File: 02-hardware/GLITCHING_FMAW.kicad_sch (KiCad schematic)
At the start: 72 parts, among them J1 USB_C_Receptacle_USB2.0_16P, J2 AIN, J3 GLITCH, J4 ANA1, J5 ANA2, J6 ANA3, J7 GND, Q2 IRLB8721PBF, U1 TLV76133, U2 TLV76133, U3 LM358, U4 RP2040, U5 W25Q128JVS, U6 MS9280, Y1 12MHz

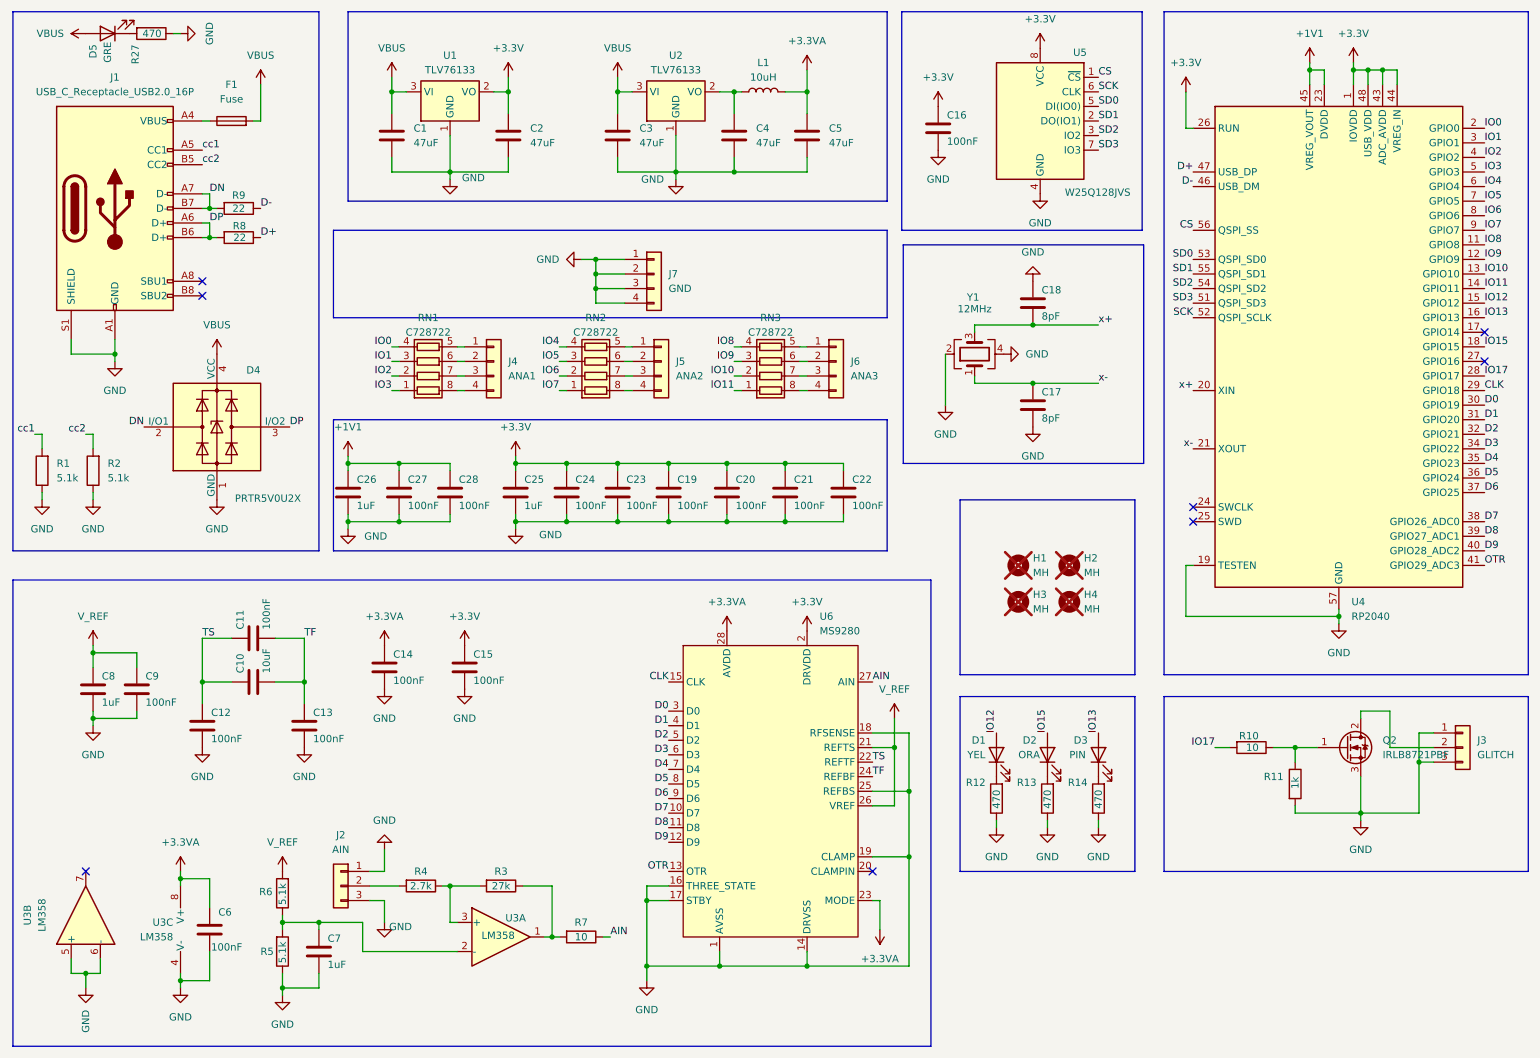
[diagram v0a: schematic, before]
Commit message: update hw to mosfet | update expamples
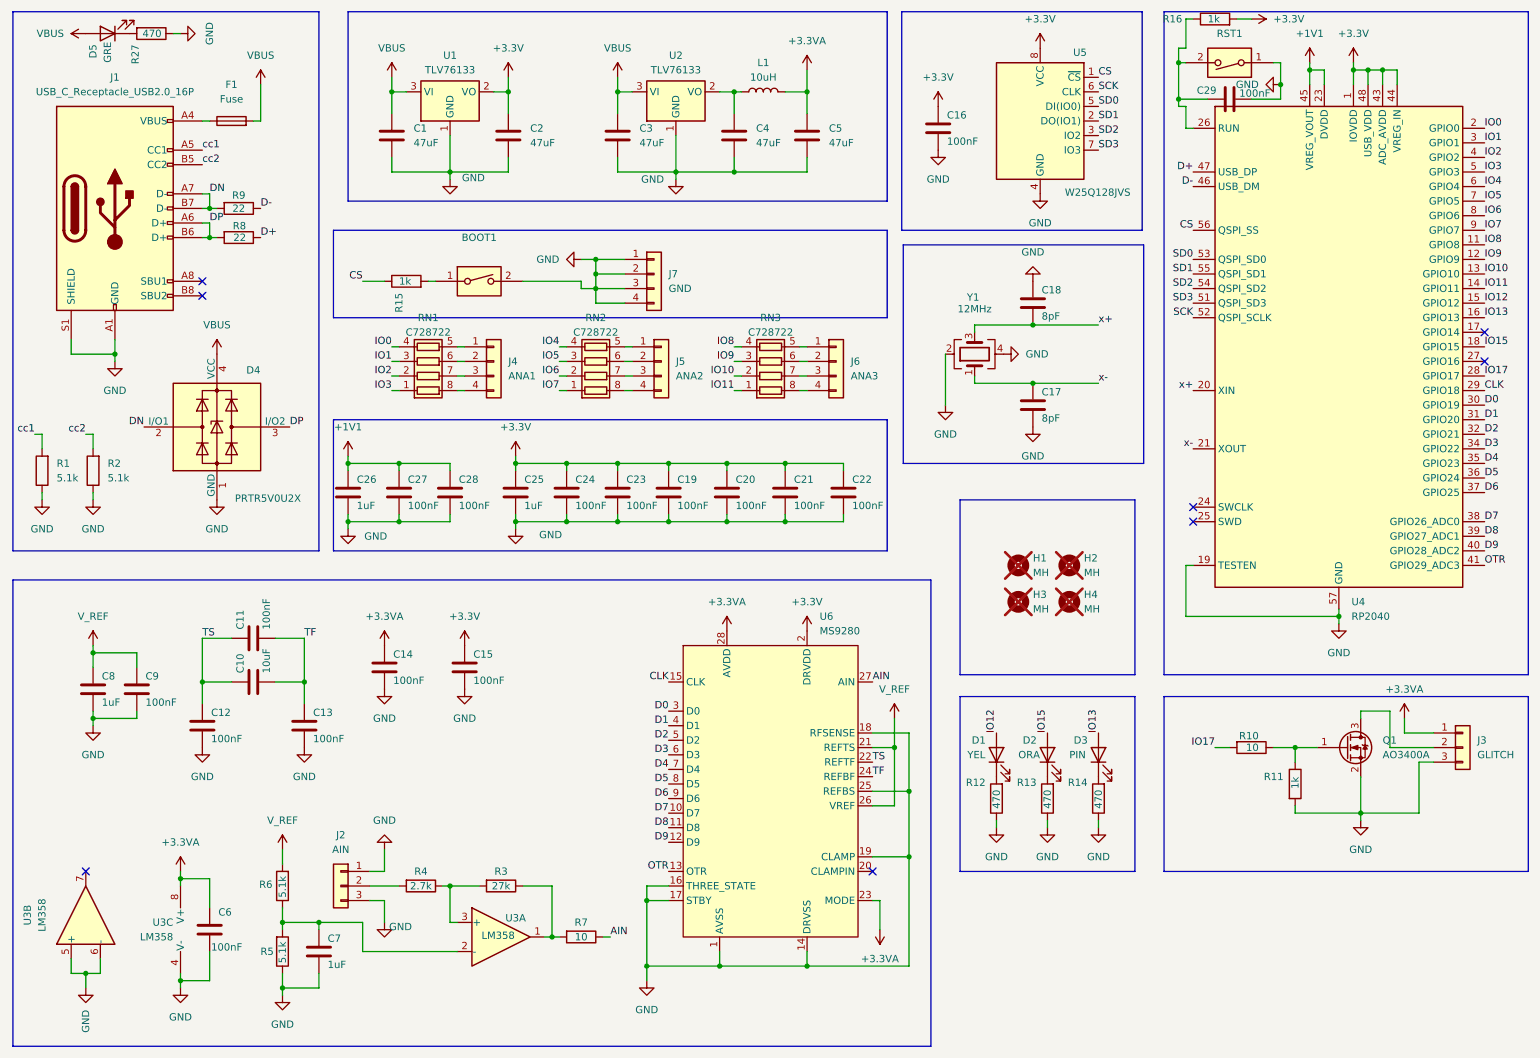
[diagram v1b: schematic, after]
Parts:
- removed Q2: IRLB8721PBF, Package_TO_SOT_SMD:SOT-223-3_TabPin2, symbol Transistor_FET:IRLB8721PBF
- added BOOT1, RST1: SW_DIP_x01, Button_Switch_SMD:SW_SPST_CK_RS282G05A3, symbol Switch:SW_DIP_x01
- added C29: 100nF, Capacitor_SMD:C_0603_1608Metric, symbol Device:C
- added Q1: AO3400A, Package_TO_SOT_SMD:SOT-23, symbol Transistor_FET:AO3400A
- added R15, R16: 1k, Resistor_SMD:R_0603_1608Metric, symbol Device:R
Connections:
- net +3.3V: now also R16.2; no longer U4.26 (RUN)
- net +3.3VA: now also J3.1 (Pin_1)
- net CS: now also R15.1
- net GND: now also BOOT1.2, C29.2, Q1.2 (S), RST1.1; no longer J3.1 (Pin_1)
- net at R10.1, R11.1: now also Q1.1 (G)
- net at J3.2 (Pin_2): now also Q1.3 (D)
- new net: C29.1, R16.1, RST1.2, U4.26 (RUN)
- new net: BOOT1.1, R15.2
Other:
- moved on the sheet: R6
